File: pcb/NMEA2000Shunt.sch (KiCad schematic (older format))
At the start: 27 parts, among them IC101 ATTINY3224-SS, P102 CONN_5, P103 CAN, U101 MCP2515, U102 TJA1050, U103 NCP1117ST50T3G, X101 8MHz

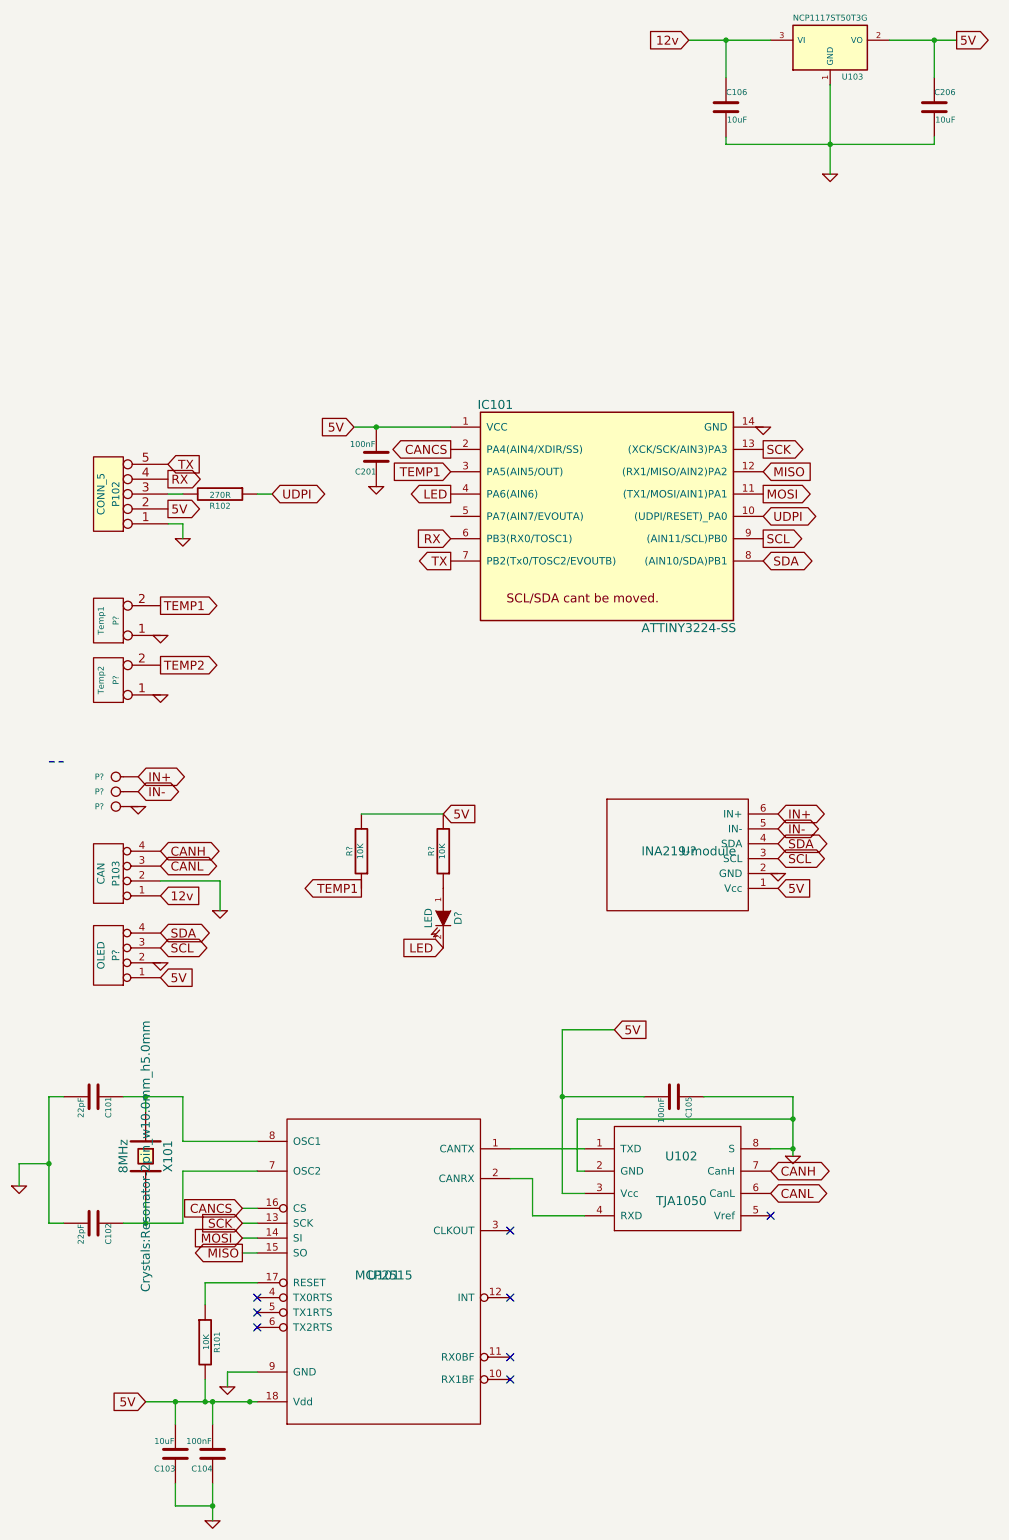
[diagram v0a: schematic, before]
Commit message: Fixed 49day overflows
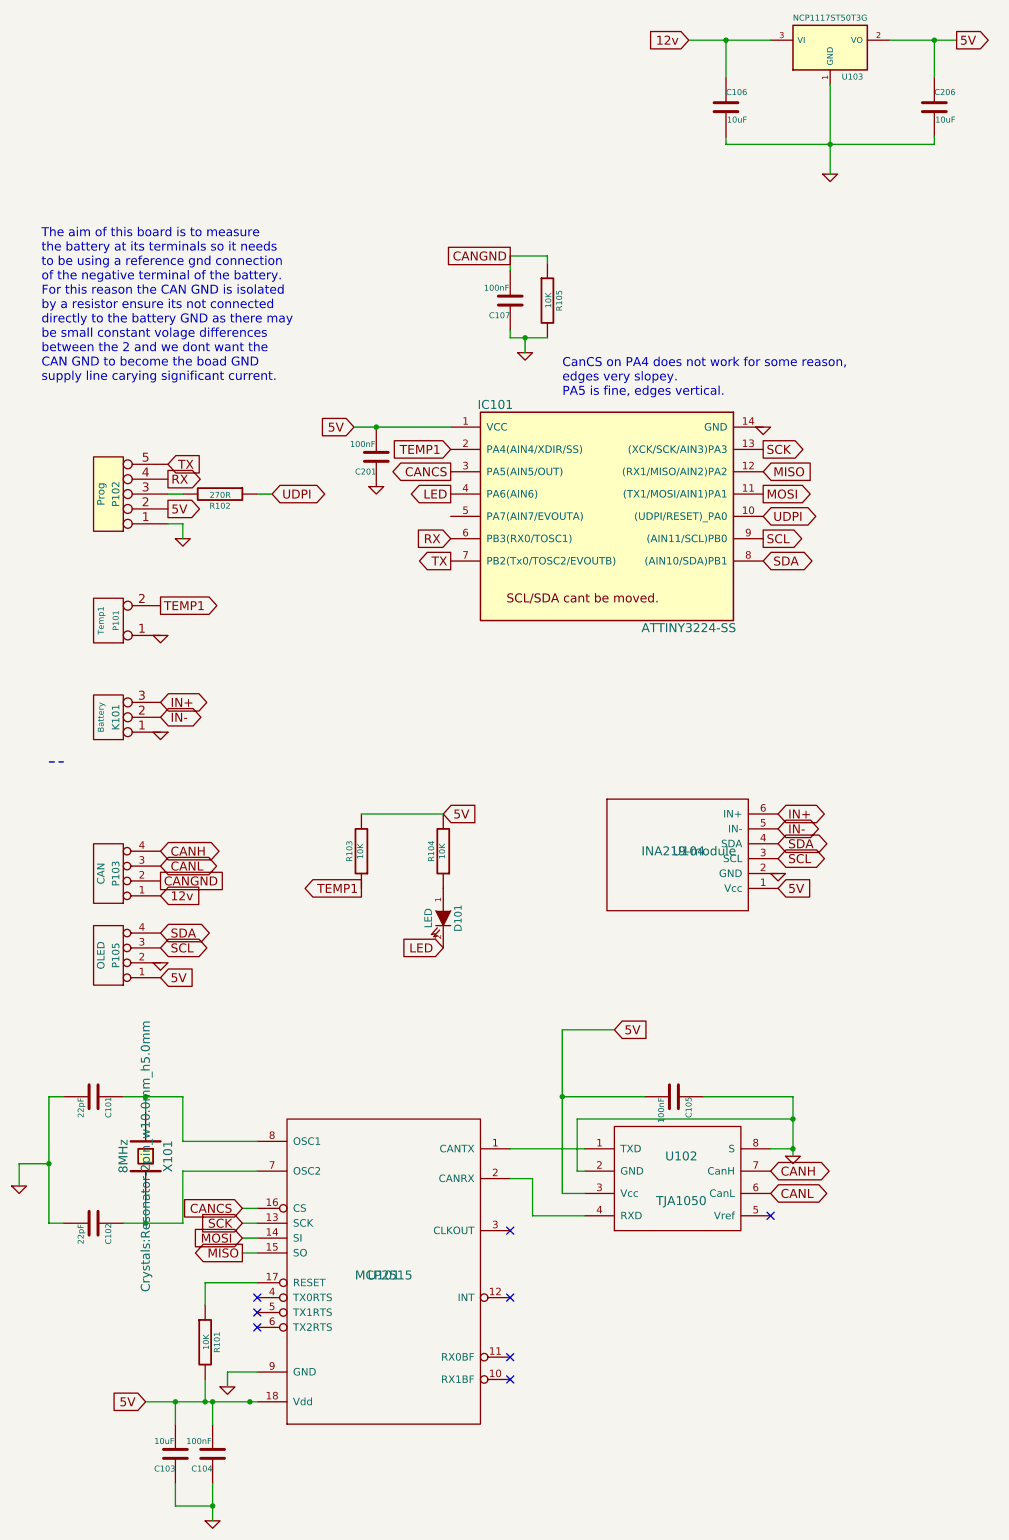
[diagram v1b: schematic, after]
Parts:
- removed P? (x3): CONN_1, symbol CONN_1
- removed P?: Temp2, symbol CONN_2
- added C107: 100nF, Capacitors_SMD:C_0805, symbol C
- added K101: Battery, Connect:bornier3, symbol CONN_3
- added R105: 10K, Resistors_SMD:R_0805_HandSoldering, symbol R
- D101: renamed from D?; footprint (none) -> LEDs:LED_0805
- P101: renamed from P?; footprint (none) -> Pin_Headers:Pin_Header_Straight_1x02
- P102: value CONN_5 -> Prog
- P105: renamed from P?; footprint Connect:bornier4 -> Pin_Headers:Pin_Header_Straight_1x04
- U104: renamed from U?; footprint (none) -> Divers:INA219Module
- gave numbers to parts that had none: 2
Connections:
- net CANCS: now also IC101.3 (PA5(AIN5/OUT)); no longer IC101.2 (PA4(AIN4/XDIR/SS))
- net GND: now also C107.1, K101.1 (P1), R105.2; no longer P103.2 (P2)
- net IN+: now also K101.3 (P3)
- net IN-: now also K101.2 (PM)
- net TEMP1: now also IC101.2 (PA4(AIN4/XDIR/SS)); no longer IC101.3 (PA5(AIN5/OUT))
- new net CANGND: C107.2, P103.2 (P2), R105.1
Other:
- note added: "CanCS on PA4 does not work for some reason,\nedges very slopey.\nPA5 is fine, edges vertical."
- note added: "The aim of this board is to measure \nthe battery at its terminals so it needs\nto be using a reference gnd connection \nof the negative terminal of the battery. \nFor this reason the CAN GND is isolated \nby a resistor ensure its not connected \ndirectly to the battery GND as there may \nbe small constant volage differences \nbetween the 2 and we dont want the \nCAN GND to become the boad GND \n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"
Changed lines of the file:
@@
 Text GLabel 5600 4050 2    60   Input ~ 0
 MISO
-Text GLabel 3500 3900 0    60   Output ~ 0
+Text GLabel 3500 4050 0    60   Output ~ 0
 CANCS
 Text GLabel 5600 4500 2    60   Output ~ 0
@@
 L GND #PWR06
 U 1 1 62C251B0
-P 1950 7000
-F 0 "#PWR06" H 1950 7000 30  0001 C CNN
-F 1 "GND" H 1950 6930 30  0001 C CNN
-F 2 "" H 1950 7000 60  0001 C CNN
-F 3 "" H 1950 7000 60  0001 C CNN
-	1    1950 7000
+P 4000 3250
+F 0 "#PWR06" H 4000 3250 30  0001 C CNN
+F 1 "GND" H 4000 3180 30  0001 C CNN
+F 2 "" H 4000 3250 60  0001 C CNN
+F 3 "" H 4000 3250 60  0001 C CNN
+	1    4000 3250
 	1    0    0    -1
 $EndComp
@@
 P 1200 4200
 F 0 "P102" V 1150 4200 50  0000 C CNN
-F 1 "CONN_5" V 1250 4200 50  0000 C CNN
+F 1 "Prog" V 1250 4200 50  0000 C CNN
 F 2 "Pin_Headers:Pin_Header_Straight_1x05" H 1200 4200 60  0001 C CNN
 F 3 "" H 1200 4200 60  0001 C CNN
@@
 $EndComp
 Wire Wire Line
-	1950 7000 1950 6800
-Wire Wire Line
-	1950 6800 1550 6800
-Wire Wire Line
 	5350 1850 6750 1850
 Wire Wire Line
@@
 	6750 1400 6750 1150
 $Comp
-L INA219-module U?
+L INA219-module U104
 U 1 1 6448C178
 P 5100 6600
-F 0 "U?" H 5100 6600 60  0000 C CNN
+F 0 "U104" H 5100 6600 60  0000 C CNN
 F 1 "INA219-module" H 5100 6600 60  0000 C CNN
-F 2 "" H 5100 6600 60  0001 C CNN
+F 2 "Divers:INA219Module" H 5100 6600 60  0001 C CNN
 F 3 "" H 5100 6600 60  0001 C CNN
 	1    5100 6600
@@
 Text GLabel 5700 6450 2    60   BiDi ~ 0
 IN-
-Text GLabel 3500 4050 0    60   Input ~ 0
+Text GLabel 3500 3900 0    60   Input ~ 0
 TEMP1
 Text GLabel 3500 4200 0    60   Output ~ 0
 LED
 $Comp
-L R R?
+L R R103
 U 1 1 6448D116
 P 2900 6600
-F 0 "R?" V 2980 6600 40  0000 C CNN
+F 0 "R103" V 2980 6600 40  0000 C CNN
 F 1 "10K" V 2907 6601 40  0000 C CNN
 F 2 "Resistors_SMD:R_0805_HandSoldering" V 2830 6600 30  0001 C CNN
@@
 $EndComp
 $Comp
-L R R?
+L R R104
 U 1 1 6448D260
 P 3450 6600
-F 0 "R?" V 3530 6600 40  0000 C CNN
+F 0 "R104" V 3530 6600 40  0000 C CNN
 F 1 "10K" V 3457 6601 40  0000 C CNN
 F 2 "Resistors_SMD:R_0805_HandSoldering" V 3380 6600 30  0001 C CNN
@@
 Wire Wire Line
 	3450 6350 2900 6350
-$Comp
-L CONN_1 P?
-U 1 1 6448D572
-P 1250 6100
-F 0 "P?" H 1330 6100 40  0000 L CNN
-F 1 "CONN_1" H 1250 6155 30  0001 C CNN
-F 2 "" H 1250 6100 60  0001 C CNN
-F 3 "" H 1250 6100 60  0001 C CNN
-	1    1250 6100
+Text GLabel 1550 5600 2    60   BiDi ~ 0
+IN+
+Text GLabel 1550 5700 2    60   BiDi ~ 0
+IN-
+$Comp
+L GND #PWR010
+U 1 1 6448D721
+P 1550 5800
+F 0 "#PWR010" H 1550 5800 30  0001 C CNN
+F 1 "GND" H 1550 5730 30  0001 C CNN
+F 2 "" H 1550 5800 60  0001 C CNN
+F 3 "" H 1550 5800 60  0001 C CNN
+	1    1550 5800
 	-1   0    0    -1
 $EndComp
 $Comp
-L CONN_1 P?
-U 1 1 6448D5EA
-P 1250 6200
-F 0 "P?" H 1330 6200 40  0000 L CNN
-F 1 "CONN_1" H 1250 6255 30  0001 C CNN
-F 2 "" H 1250 6200 60  0001 C CNN
-F 3 "" H 1250 6200 60  0001 C CNN
-	1    1250 6200
-	-1   0    0    -1
-$EndComp
-$Comp
-L CONN_1 P?
-U 1 1 6448D640
-P 1250 6300
-F 0 "P?" H 1330 6300 40  0000 L CNN
-F 1 "CONN_1" H 1250 6355 30  0001 C CNN
-F 2 "" H 1250 6300 60  0001 C CNN
-F 3 "" H 1250 6300 60  0001 C CNN
-	1    1250 6300
-	-1   0    0    -1
-$EndComp
-Text GLabel 1400 6100 2    60   BiDi ~ 0
-IN+
-Text GLabel 1400 6200 2    60   BiDi ~ 0
-IN-
-$Comp
-L GND #PWR?
-U 1 1 6448D721
-P 1400 6300
-F 0 "#PWR?" H 1400 6300 30  0001 C CNN
-F 1 "GND" H 1400 6230 30  0001 C CNN
-F 2 "" H 1400 6300 60  0001 C CNN
-F 3 "" H 1400 6300 60  0001 C CNN
-	1    1400 6300
-	-1   0    0    -1
-$EndComp
-$Comp
-L CONN_4 P?
+L CONN_4 P105
 U 1 1 6448D7CD
 P 1200 7300
-F 0 "P?" V 1150 7300 50  0000 C CNN
+F 0 "P105" V 1150 7300 50  0000 C CNN
 F 1 "OLED" V 1250 7300 50  0000 C CNN
-F 2 "Connect:bornier4" H 1200 7300 60  0001 C CNN
+F 2 "Pin_Headers:Pin_Header_Straight_1x04" H 1200 7300 60  0001 C CNN
 F 3 "" H 1200 7300 60  0001 C CNN
 	1    1200 7300
@@
 SCL
 $Comp
-L GND #PWR?
+L GND #PWR011
 U 1 1 6448D8EF
 P 1550 7350
-F 0 "#PWR?" H 1550 7350 30  0001 C CNN
+F 0 "#PWR011" H 1550 7350 30  0001 C CNN
 F 1 "GND" H 1550 7280 30  0001 C CNN
 F 2 "" H 1550 7350 60  0001 C CNN
@@
 5V
 $Comp
-L CONN_2 P?
+L CONN_2 P101
 U 1 1 6448DB6A
 P 1200 5050
-F 0 "P?" V 1150 5050 40  0000 C CNN
+F 0 "P101" V 1150 5050 40  0000 C CNN
 F 1 "Temp1" V 1250 5050 40  0000 C CNN
-F 2 "" H 1200 5050 60  0001 C CNN
+F 2 "Pin_Headers:Pin_Header_Straight_1x02" H 1200 5050 60  0001 C CNN
 F 3 "" H 1200 5050 60  0001 C CNN
 	1    1200 5050
@@
 TEMP1
 $Comp
-L CONN_2 P?
-U 1 1 6448DC32
-P 1200 5450
-F 0 "P?" V 1150 5450 40  0000 C CNN
-F 1 "Temp2" V 1250 5450 40  0000 C CNN
-F 2 "" H 1200 5450 60  0001 C CNN
-F 3 "" H 1200 5450 60  0001 C CNN
-	1    1200 5450
-	-1   0    0    1
-$EndComp
-Text GLabel 1550 5350 2    60   Output ~ 0
-TEMP2
-$Comp
-L GND #PWR?
+L GND #PWR012
 U 1 1 6448DD33
 P 1550 5150
-F 0 "#PWR?" H 1550 5150 30  0001 C CNN
+F 0 "#PWR012" H 1550 5150 30  0001 C CNN
 F 1 "GND" H 1550 5080 30  0001 C CNN
 F 2 "" H 1550 5150 60  0001 C CNN
@@
 	1    0    0    -1
 $EndComp
-$Comp
-L GND #PWR?
-U 1 1 6448DD8C
-P 1550 5550
-F 0 "#PWR?" H 1550 5550 30  0001 C CNN
-F 1 "GND" H 1550 5480 30  0001 C CNN
-F 2 "" H 1550 5550 60  0001 C CNN
-F 3 "" H 1550 5550 60  0001 C CNN
-	1    1550 5550
-	1    0    0    -1
-$EndComp
 Connection ~ 3000 3750
 $Comp
-L GND #PWR?
+L GND #PWR013
 U 1 1 6448E6C2
 P 3000 4150
-F 0 "#PWR?" H 3000 4150 30  0001 C CNN
+F 0 "#PWR013" H 3000 4150 30  0001 C CNN
 F 1 "GND" H 3000 4080 30  0001 C CNN
 F 2 "" H 3000 4150 60  0001 C CNN
@@
 $EndComp
 $Comp
-L LED D?
+L LED D101
 U 1 1 644D43C8
 P 3450 7050
-F 0 "D?" H 3450 7150 50  0000 C CNN
+F 0 "D101" H 3450 7150 50  0000 C CNN
 F 1 "LED" H 3450 6950 50  0000 C CNN
-F 2 "" H 3450 7050 60  0000 C CNN
+F 2 "LEDs:LED_0805" H 3450 7050 60  0001 C CNN
 F 3 "" H 3450 7050 60  0000 C CNN
 	1    3450 7050
 	0    1    1    0
 $EndComp
+$Comp
+L CONN_3 K101
+U 1 1 644D4D79
+P 1200 5700
+F 0 "K101" V 1150 5700 50  0000 C CNN
+F 1 "Battery" V 1250 5700 40  0000 C CNN
+F 2 "Connect:bornier3" H 1200 5700 60  0001 C CNN
+F 3 "" H 1200 5700 60  0001 C CNN
+	1    1200 5700
+	-1   0    0    1
+$EndComp
+$Comp
+L R R105
+U 1 1 644E00AC
+P 4150 2900
+F 0 "R105" V 4230 2900 40  0000 C CNN
+F 1 "10K" V 4157 2901 40  0000 C CNN
+F 2 "Resistors_SMD:R_0805_HandSoldering" V 4080 2900 30  0001 C CNN
+F 3 "" H 4150 2900 30  0000 C CNN
+	1    4150 2900
+	1    0    0    -1
+$EndComp
+Text Notes 750  3450 0    60   ~ 0
+The aim of this board is to measure \nthe battery at its terminals so it needs\nto be using a reference gnd connection \nof the negative terminal of the battery. \nFor this reason the CAN GND is isolated \nby a resistor ensure its not connected \ndirectly to the battery GND as there may \nbe small constant volage differences \nbetween the 2 and we dont want the \nCAN GND to become the boad GND \nsupply line carying significant current.
+$Comp
+L C C107
+U 1 1 644E044D
+P 3900 2900
+F 0 "C107" H 3900 3000 40  0000 L CNN
+F 1 "100nF" H 3906 2815 40  0000 L CNN
+F 2 "Capacitors_SMD:C_0805" H 3938 2750 30  0001 C CNN
+F 3 "" H 3900 2900 60  0000 C CNN
+	1    3900 2900
+	-1   0    0    1
+$EndComp
+Wire Wire Line
+	3900 2700 3900 2600
+Wire Wire Line
+	3900 2600 4150 2600
+Wire Wire Line
+	4150 2600 4150 2650
+Wire Wire Line
+	3900 3150 4150 3150
+Wire Wire Line
+	3900 3150 3900 3100
+Wire Wire Line
+	4000 3150 4000 3250
+Connection ~ 4000 3150
+Text GLabel 3900 2600 0    60   UnSpc ~ 0
+CANGND
+Text GLabel 1550 6800 2    60   UnSpc ~ 0
+CANGND
+Text Notes 4250 3550 0    60   ~ 0
+CanCS on PA4 does not work for some reason,\nedges very slopey.\nPA5 is fine, edges vertical.
 $EndSCHEMATC
